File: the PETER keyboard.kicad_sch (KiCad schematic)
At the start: 16 parts

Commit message: starting to set up matrix
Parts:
- added D? (x58): D_Small, symbol Device:D_Small
- added MX? (x58): MX-NoLED, symbol MX_Alps_Hybrid:MX-NoLED
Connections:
- new net: D?.2 (A), MX?.2 (ROW) (x58)

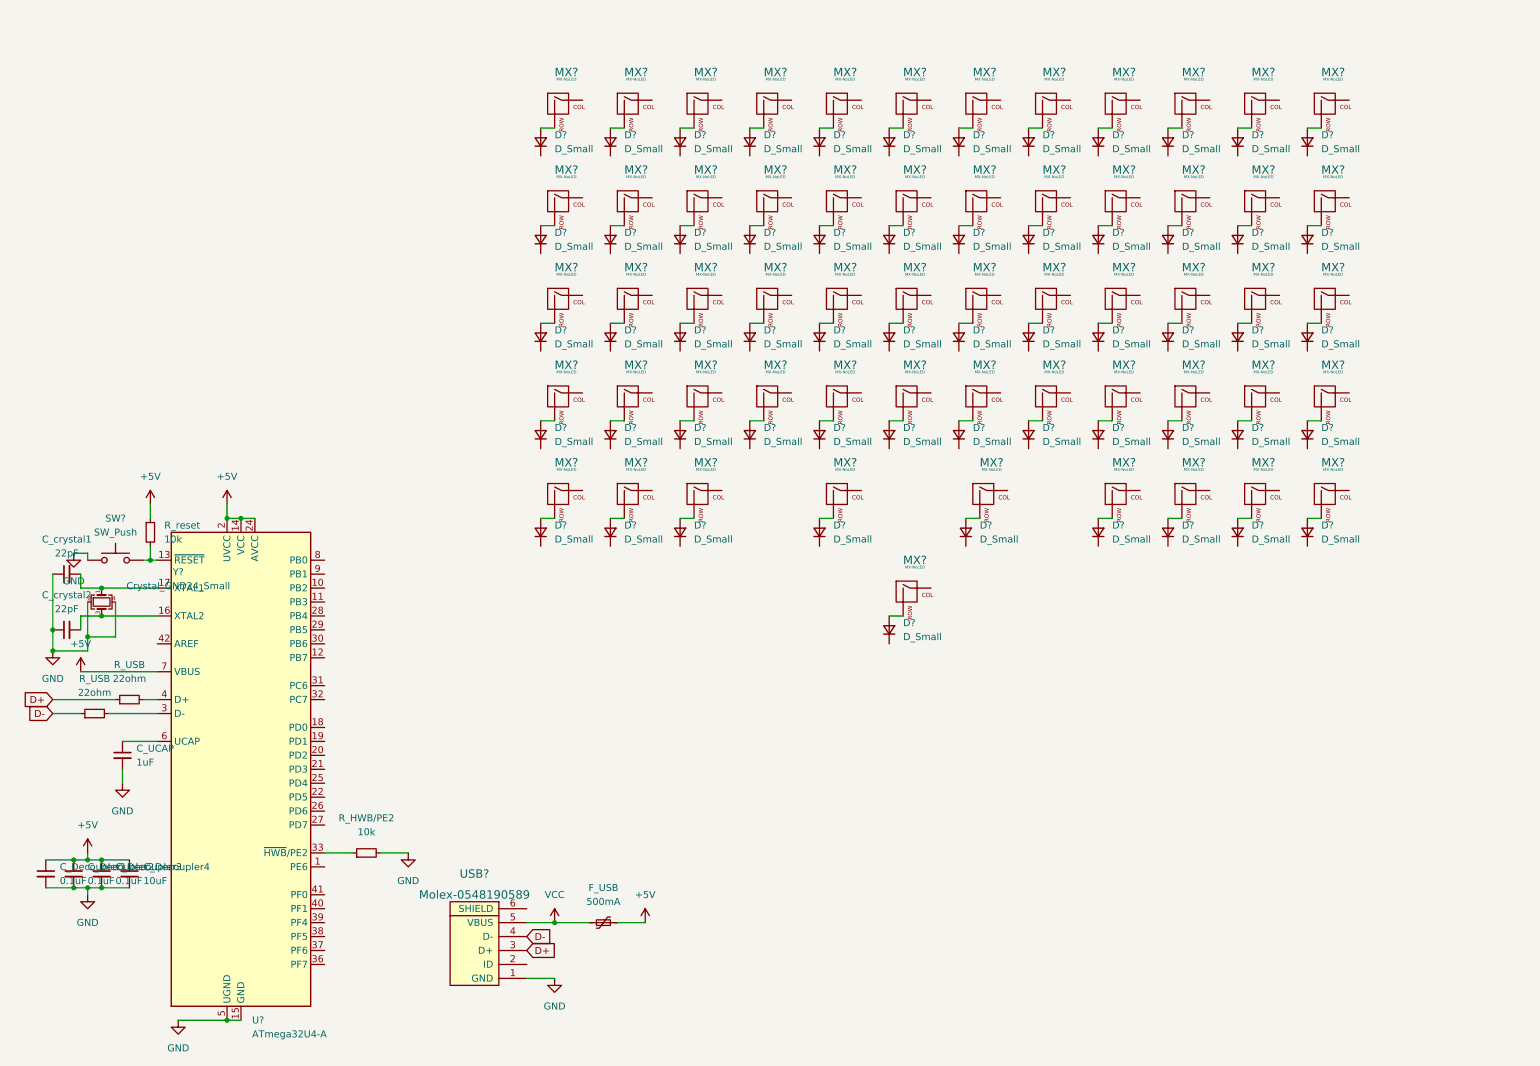
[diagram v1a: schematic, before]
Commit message: switch matrix set up complete
whole switch matrix,

but no rotary encoders yet,

no usb c
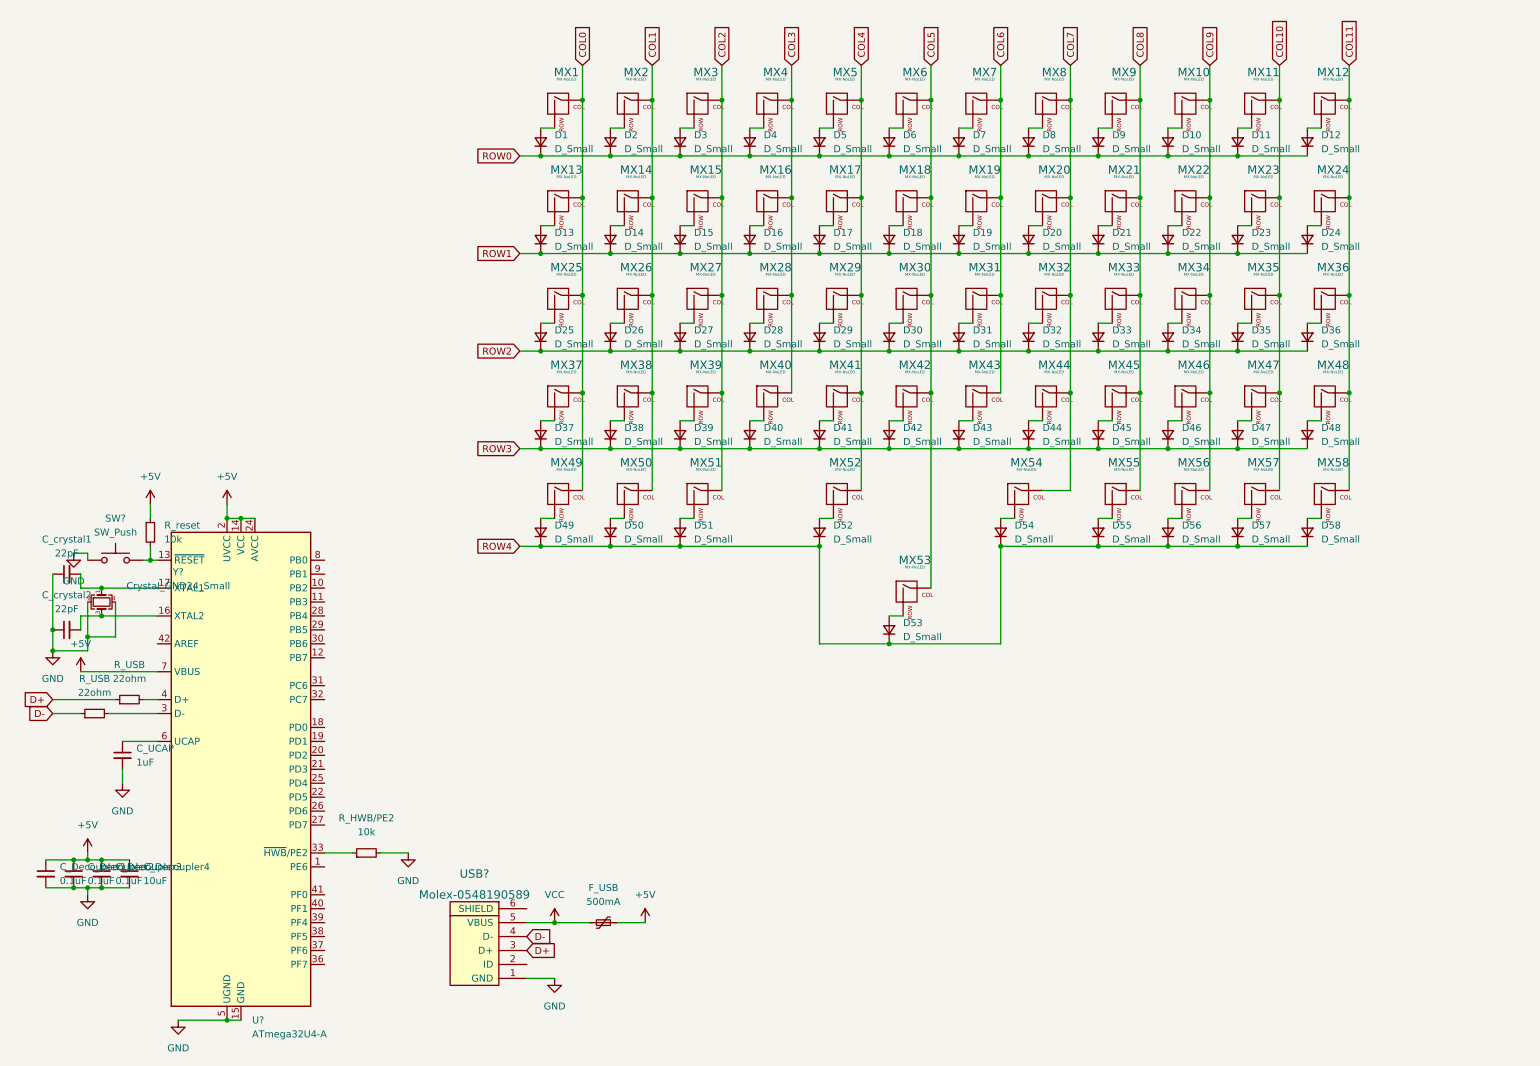
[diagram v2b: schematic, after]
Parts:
- gave numbers to parts that had none: 116
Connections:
- net ROW0: now reaches D10.1 (K)
- net ROW0: now also D1.1 (K), D11.1 (K), D12.1 (K), D2.1 (K), D3.1 (K), D4.1 (K), D5.1 (K), D6.1 (K), D7.1 (K), D8.1 (K), D9.1 (K)
- net ROW4: now reaches D50.1 (K)
- net ROW4: now also D49.1 (K), D51.1 (K), D52.1 (K), D53.1 (K), D54.1 (K), D55.1 (K), D56.1 (K), D57.1 (K), D58.1 (K)
- net  ROW3: now reaches D44.1 (K)
- net  ROW3: now also D37.1 (K), D38.1 (K), D39.1 (K), D40.1 (K), D41.1 (K), D42.1 (K), D43.1 (K), D45.1 (K), D46.1 (K), D47.1 (K), D48.1 (K)
- net ROW2: now reaches D28.1 (K)
- net ROW2: now also D25.1 (K), D26.1 (K), D27.1 (K), D29.1 (K), D30.1 (K), D31.1 (K), D32.1 (K), D33.1 (K), D34.1 (K), D35.1 (K), D36.1 (K)
- net COL9: now reaches MX10.1 (COL)
- net COL9: now also MX22.1 (COL), MX34.1 (COL), MX46.1 (COL), MX56.1 (COL)
- net COL5: now reaches MX53.1 (COL)
- net COL5: now also MX18.1 (COL), MX30.1 (COL), MX42.1 (COL), MX6.1 (COL)
- net COL2: now reaches MX51.1 (COL)
- net COL2: now also MX15.1 (COL), MX27.1 (COL), MX3.1 (COL), MX39.1 (COL)
- net COL10: now reaches MX23.1 (COL)
- net COL10: now also MX11.1 (COL), MX35.1 (COL), MX47.1 (COL), MX57.1 (COL)
- net COL7: now reaches MX54.1 (COL)
- net COL7: now also MX20.1 (COL), MX32.1 (COL), MX44.1 (COL), MX8.1 (COL)
- net COL4: now reaches MX17.1 (COL)
- net COL4: now also MX29.1 (COL), MX41.1 (COL), MX5.1 (COL), MX52.1 (COL)
- net ROW1: now reaches D13.1 (K)
- net ROW1: now also D14.1 (K), D15.1 (K), D16.1 (K), D17.1 (K), D18.1 (K), D19.1 (K), D20.1 (K), D21.1 (K), D22.1 (K), D23.1 (K), D24.1 (K)
- net COL8: now reaches MX33.1 (COL)
- net COL8: now also MX21.1 (COL), MX45.1 (COL), MX55.1 (COL), MX9.1 (COL)
- net COL0: now reaches MX37.1 (COL)
- net COL0: now also MX1.1 (COL), MX13.1 (COL), MX25.1 (COL), MX49.1 (COL)
- net COL11: now reaches MX12.1 (COL)
- net COL11: now also MX24.1 (COL), MX36.1 (COL), MX48.1 (COL), MX58.1 (COL)
- net COL6: now reaches MX43.1 (COL)
- net COL6: now also MX19.1 (COL), MX31.1 (COL), MX7.1 (COL)
- net COL1: now reaches MX26.1 (COL)
- net COL1: now also MX14.1 (COL), MX2.1 (COL), MX38.1 (COL), MX50.1 (COL)
- net COL3: now reaches MX40.1 (COL)
- net COL3: now also MX16.1 (COL), MX28.1 (COL), MX4.1 (COL)
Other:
- moved on the sheet: D54, MX54

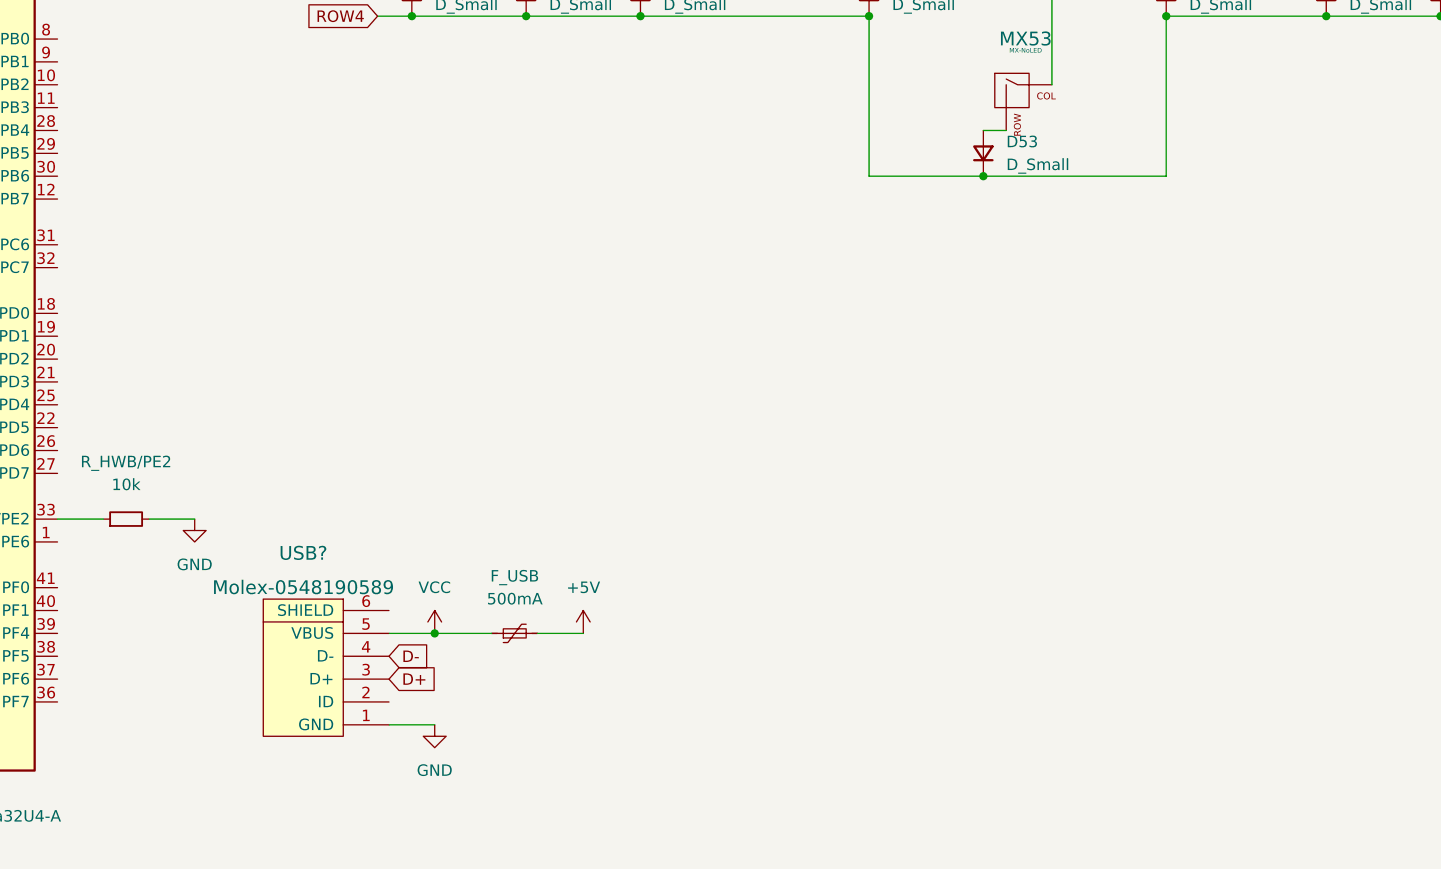
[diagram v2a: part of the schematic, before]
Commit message: schematics for USB C added
shielding not complete
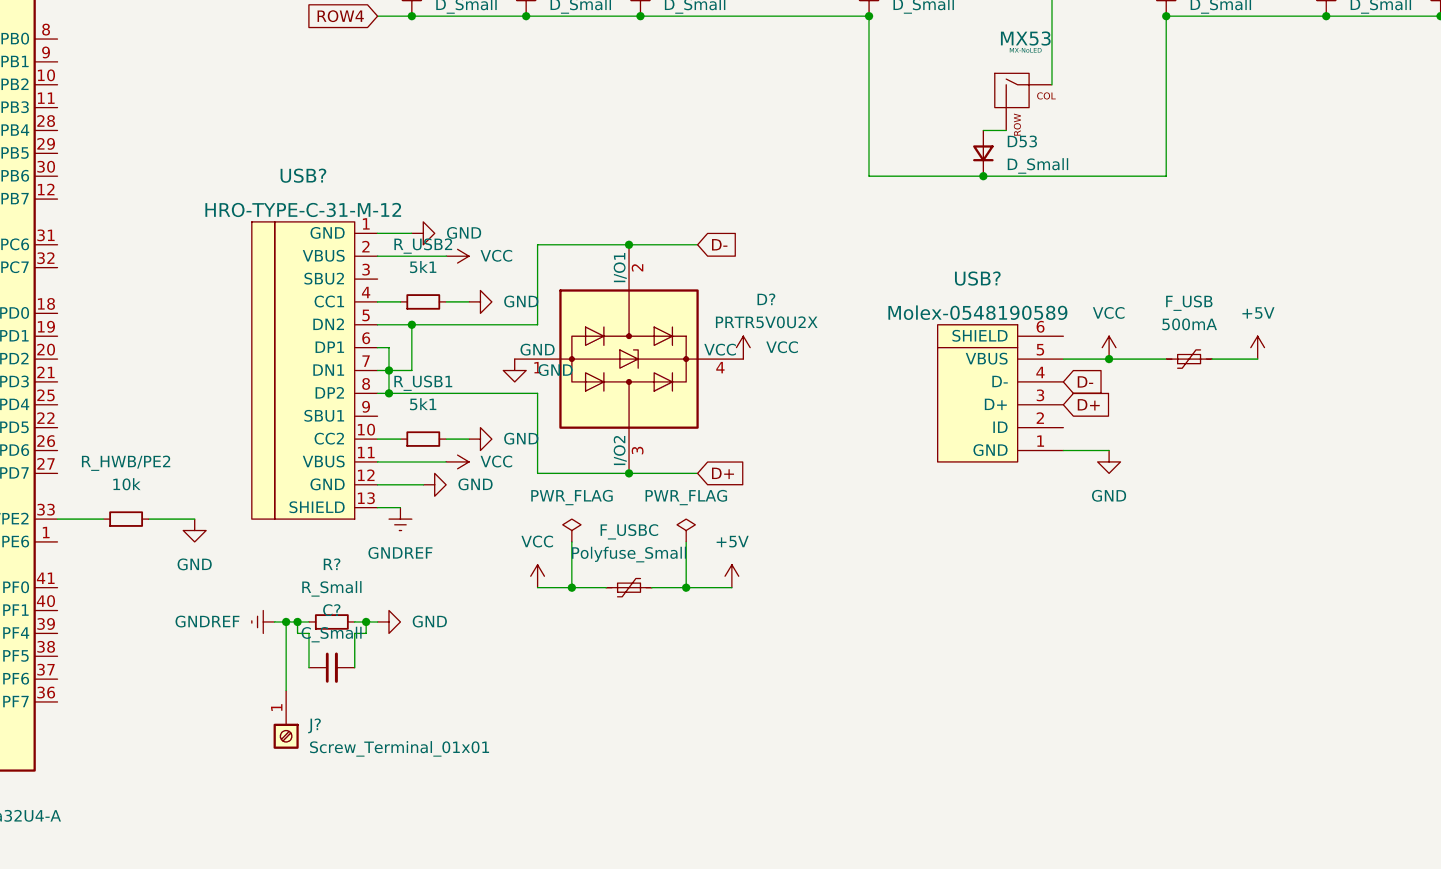
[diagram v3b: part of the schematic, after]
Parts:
- added C?: C_Small, symbol Device:C_Small
- added D?: PRTR5V0U2X, Package_TO_SOT_SMD:SOT-143, symbol Power_Protection:PRTR5V0U2X
- added F_USBC: Polyfuse_Small, symbol Device:Polyfuse_Small
- added J?: Screw_Terminal_01x01, symbol Connector:Screw_Terminal_01x01
- added R?: R_Small, symbol Device:R_Small
- added R_USB1, R_USB2: 5k1, symbol Device:R_Small
- added USB?: HRO-TYPE-C-31-M-12, symbol keebio:HRO-TYPE-C-31-M-12
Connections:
- net D- is gone; now on net D+: R_USB.1, USB?.4 (D-)
- net +5V: now also F_USBC.2
- net D+: now also D?.2 (I/O1), D?.3 (I/O2), USB?.5 (DN2), USB?.6 (DP1), USB?.7 (DN1), USB?.8 (DP2)
- net GND: now also C?.2, D?.1 (GND), R?.2, R_USB1.2, R_USB2.2, USB?.1 (GND), USB?.12 (GND)
- net VCC: now also D?.4 (VCC), F_USBC.1, USB?.11 (VBUS), USB?.2 (VBUS)
- new net: R_USB1.1, USB?.10 (CC2)
- new net: R_USB2.1, USB?.4 (CC1)
- new net GNDREF: C?.1, J?.1 (Pin_1), R?.1, USB?.13 (SHIELD)
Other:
- moved on the sheet: F_USB, USB?
